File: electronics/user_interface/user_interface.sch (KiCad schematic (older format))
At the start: 87 parts, among them J1 Conn_01x06, J2 Conn_02x05_Odd_Even, SW1 ALPS_EC11E18244A5, U1 PCF8574, U2 PCF8574

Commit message: updated footprints to include 3dmodel of SOD-523 diode
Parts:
- N1: footprint Symbols:OSHW-Symbol_6.7x6mm_SilkScreen -> Symbol:OSHW-Symbol_6.7x6mm_SilkScreen
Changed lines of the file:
@@
 F 0 "N1" H 9450 6150 60  0000 C CNN
 F 1 "OHWLOGO" H 9450 5850 60  0000 C CNN
-F 2 "Symbols:OSHW-Symbol_6.7x6mm_SilkScreen" H 9450 6000 60  0001 C CNN
+F 2 "Symbol:OSHW-Symbol_6.7x6mm_SilkScreen" H 9450 6000 60  0001 C CNN
 F 3 "" H 9450 6000 60  0001 C CNN
 	1    9450 6000

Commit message: updated versionnumber
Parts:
- N2: value V20200517 -> V20200521
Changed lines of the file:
@@
 P 9450 6350
 F 0 "N2" H 9450 6450 60  0000 C CNN
-F 1 "V20200517" H 9450 6350 60  0000 C CNN
+F 1 "V20200521" H 9450 6350 60  0000 C CNN
 F 2 "SquantorLabels:Label_Generic" H 9450 6350 60  0001 C CNN
 F 3 "" H 9450 6350 60  0001 C CNN

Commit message: added pullup resistors, updated versionnumber
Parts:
- added R? (x2): 4.7K, SquantorRcl:R_0603_hand, symbol Device:R
- N2: value V20200521 -> V20200522
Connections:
- net SCL: now also R?.1
- net SDA: now also R?.1
- net VDD: now also R?.2, R?.2
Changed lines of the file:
@@
 P 9450 6350
 F 0 "N2" H 9450 6450 60  0000 C CNN
-F 1 "V20200521" H 9450 6350 60  0000 C CNN
+F 1 "V20200522" H 9450 6350 60  0000 C CNN
 F 2 "SquantorLabels:Label_Generic" H 9450 6350 60  0001 C CNN
 F 3 "" H 9450 6350 60  0001 C CNN
@@
 Wire Notes Line
 	2100 2400 2100 2550
+Text Label 2700 2150 0    50   ~ 0
+SDA
+Text Label 2700 2250 0    50   ~ 0
+SCL
+$Comp
+L Device:R R?
+U 1 1 5EC93454
+P 2500 2150
+F 0 "R?" V 2450 2000 50  0000 C CNN
+F 1 "4.7K" V 2500 2150 50  0000 C CNN
+F 2 "SquantorRcl:R_0603_hand" V 2430 2150 50  0001 C CNN
+F 3 "~" H 2500 2150 50  0001 C CNN
+	1    2500 2150
+	0    1    1    0
+$EndComp
+$Comp
+L Device:R R?
+U 1 1 5EC9375B
+P 2500 2250
+F 0 "R?" V 2450 2100 50  0000 C CNN
+F 1 "4.7K" V 2500 2250 50  0000 C CNN
+F 2 "SquantorRcl:R_0603_hand" V 2430 2250 50  0001 C CNN
+F 3 "~" H 2500 2250 50  0001 C CNN
+	1    2500 2250
+	0    1    1    0
+$EndComp
+Text Label 2300 2150 2    50   ~ 0
+VDD
+Text Label 2300 2250 2    50   ~ 0
+VDD
+Wire Wire Line
+	2300 2150 2350 2150
+Wire Wire Line
+	2350 2250 2300 2250
+Wire Wire Line
+	2700 2150 2650 2150
+Wire Wire Line
+	2650 2250 2700 2250
 $EndSCHEMATC

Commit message: routing completed
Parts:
- added R46: 4.7K, SquantorRcl:R_0603_hand, symbol Device:R
- gave numbers to parts that had none: 2
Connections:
- net !INT: now also R46.1
- net VDD: now also R46.2
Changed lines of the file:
@@
 SCL
 $Comp
-L Device:R R?
+L Device:R R44
 U 1 1 5EC93454
 P 2500 2150
-F 0 "R?" V 2450 2000 50  0000 C CNN
+F 0 "R44" V 2450 2000 50  0000 C CNN
 F 1 "4.7K" V 2500 2150 50  0000 C CNN
 F 2 "SquantorRcl:R_0603_hand" V 2430 2150 50  0001 C CNN
@@
 $EndComp
 $Comp
-L Device:R R?
+L Device:R R45
 U 1 1 5EC9375B
 P 2500 2250
-F 0 "R?" V 2450 2100 50  0000 C CNN
+F 0 "R45" V 2450 2100 50  0000 C CNN
 F 1 "4.7K" V 2500 2250 50  0000 C CNN
 F 2 "SquantorRcl:R_0603_hand" V 2430 2250 50  0001 C CNN
@@
 Wire Wire Line
 	2650 2250 2700 2250
+$Comp
+L Device:R R46
+U 1 1 5ED00DE2
+P 2500 2350
+F 0 "R46" V 2450 2200 50  0000 C CNN
+F 1 "4.7K" V 2500 2350 50  0000 C CNN
+F 2 "SquantorRcl:R_0603_hand" V 2430 2350 50  0001 C CNN
+F 3 "~" H 2500 2350 50  0001 C CNN
+	1    2500 2350
+	0    1    1    0
+$EndComp
+Text Label 2700 2350 0    50   ~ 0
+!INT
+Text Label 2300 2350 2    50   ~ 0
+VDD
+Wire Wire Line
+	2300 2350 2350 2350
+Wire Wire Line
+	2650 2350 2700 2350
 $EndSCHEMATC

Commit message: updated versionnumber, changed address selection tracks so you could disconnect them by cutting traces
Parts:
- N2: value V20200522 -> V20200524
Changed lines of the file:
@@
 P 9450 6350
 F 0 "N2" H 9450 6450 60  0000 C CNN
-F 1 "V20200522" H 9450 6350 60  0000 C CNN
+F 1 "V20200524" H 9450 6350 60  0000 C CNN
 F 2 "SquantorLabels:Label_Generic" H 9450 6350 60  0001 C CNN
 F 3 "" H 9450 6350 60  0001 C CNN

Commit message: added buzzer circuit
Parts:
- added BZ1: Buzzer, Buzzer_Beeper:Buzzer_12x9.5RM7.6, symbol Device:Buzzer
- N2: value V20200524 -> V20200602
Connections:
- net VDD: now also BZ1.1 (-); no longer R25.1
- new net Buzzer: BZ1.2 (+), R25.1
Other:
- moved on the sheet: R25
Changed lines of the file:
@@
 P 9450 6350
 F 0 "N2" H 9450 6450 60  0000 C CNN
-F 1 "V20200524" H 9450 6350 60  0000 C CNN
+F 1 "V20200602" H 9450 6350 60  0000 C CNN
 F 2 "SquantorLabels:Label_Generic" H 9450 6350 60  0001 C CNN
 F 3 "" H 9450 6350 60  0001 C CNN
@@
 	1    0    0    -1
 $EndComp
-Text Label 10800 3800 0    50   ~ 0
-VDD
 Wire Wire Line
 	10150 3900 10100 3900
@@
 	11000 3150 11000 5600
 Wire Wire Line
-	10100 3800 10450 3800
-Wire Wire Line
-	10750 3800 10800 3800
+	10100 3800 10200 3800
+Wire Wire Line
+	10500 3800 10550 3800
 $Comp
 L Device:R R25
 U 1 1 5ED82CF1
-P 10600 3800
-F 0 "R25" V 10550 3650 50  0000 C CNN
-F 1 "4.7K" V 10600 3800 50  0000 C CNN
-F 2 "SquantorRcl:R_0603_hand" V 10530 3800 50  0001 C CNN
-F 3 "~" H 10600 3800 50  0001 C CNN
-	1    10600 3800
+P 10350 3800
+F 0 "R25" V 10300 3650 50  0000 C CNN
+F 1 "4.7K" V 10350 3800 50  0000 C CNN
+F 2 "SquantorRcl:R_0603_hand" V 10280 3800 50  0001 C CNN
+F 3 "~" H 10350 3800 50  0001 C CNN
+	1    10350 3800
 	0    1    1    0
 $EndComp
@@
 Wire Wire Line
 	2650 2350 2700 2350
+$Comp
+L Device:Buzzer BZ1
+U 1 1 5ED89C6E
+P 6250 6950
+F 0 "BZ1" H 6402 6979 50  0000 L CNN
+F 1 "Buzzer" H 6402 6888 50  0000 L CNN
+F 2 "Buzzer_Beeper:Buzzer_12x9.5RM7.6" V 6225 7050 50  0001 C CNN
+F 3 "~" V 6225 7050 50  0001 C CNN
+	1    6250 6950
+	1    0    0    -1
+$EndComp
+Text Label 6100 6850 2    50   ~ 0
+VDD
+Wire Wire Line
+	6100 6850 6150 6850
+Text Label 10550 3800 0    50   ~ 0
+Buzzer
+Text Label 6100 7050 2    50   ~ 0
+Buzzer
+Wire Wire Line
+	6100 7050 6150 7050
 $EndSCHEMATC

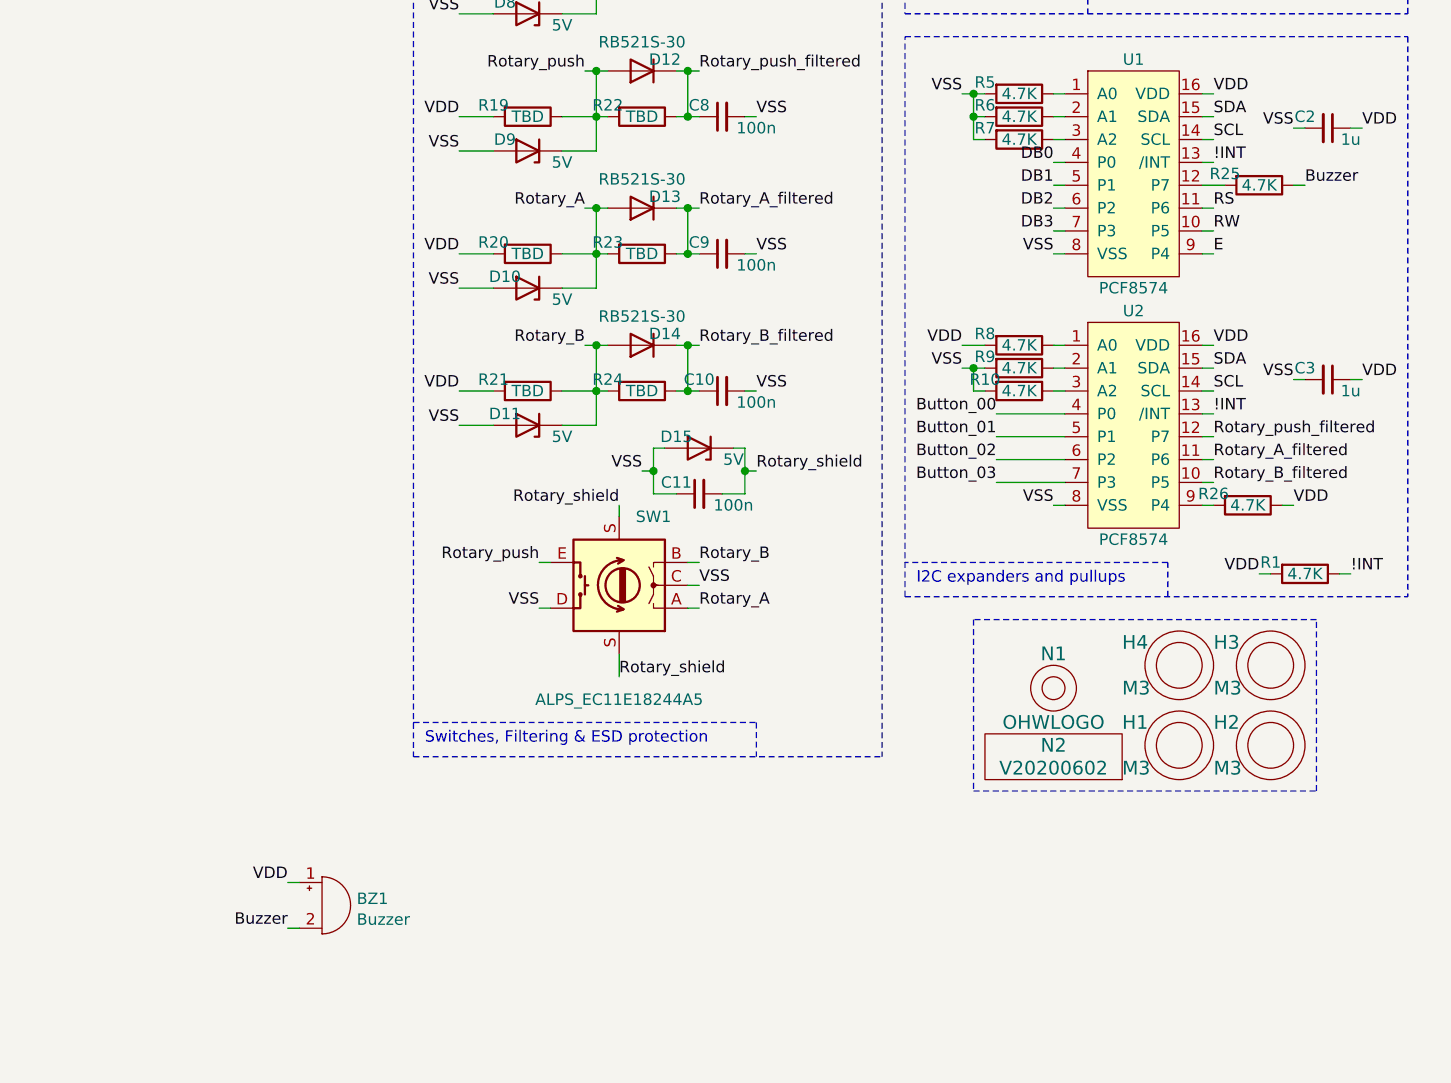
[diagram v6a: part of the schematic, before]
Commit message: prettyfied the buzzer circuit
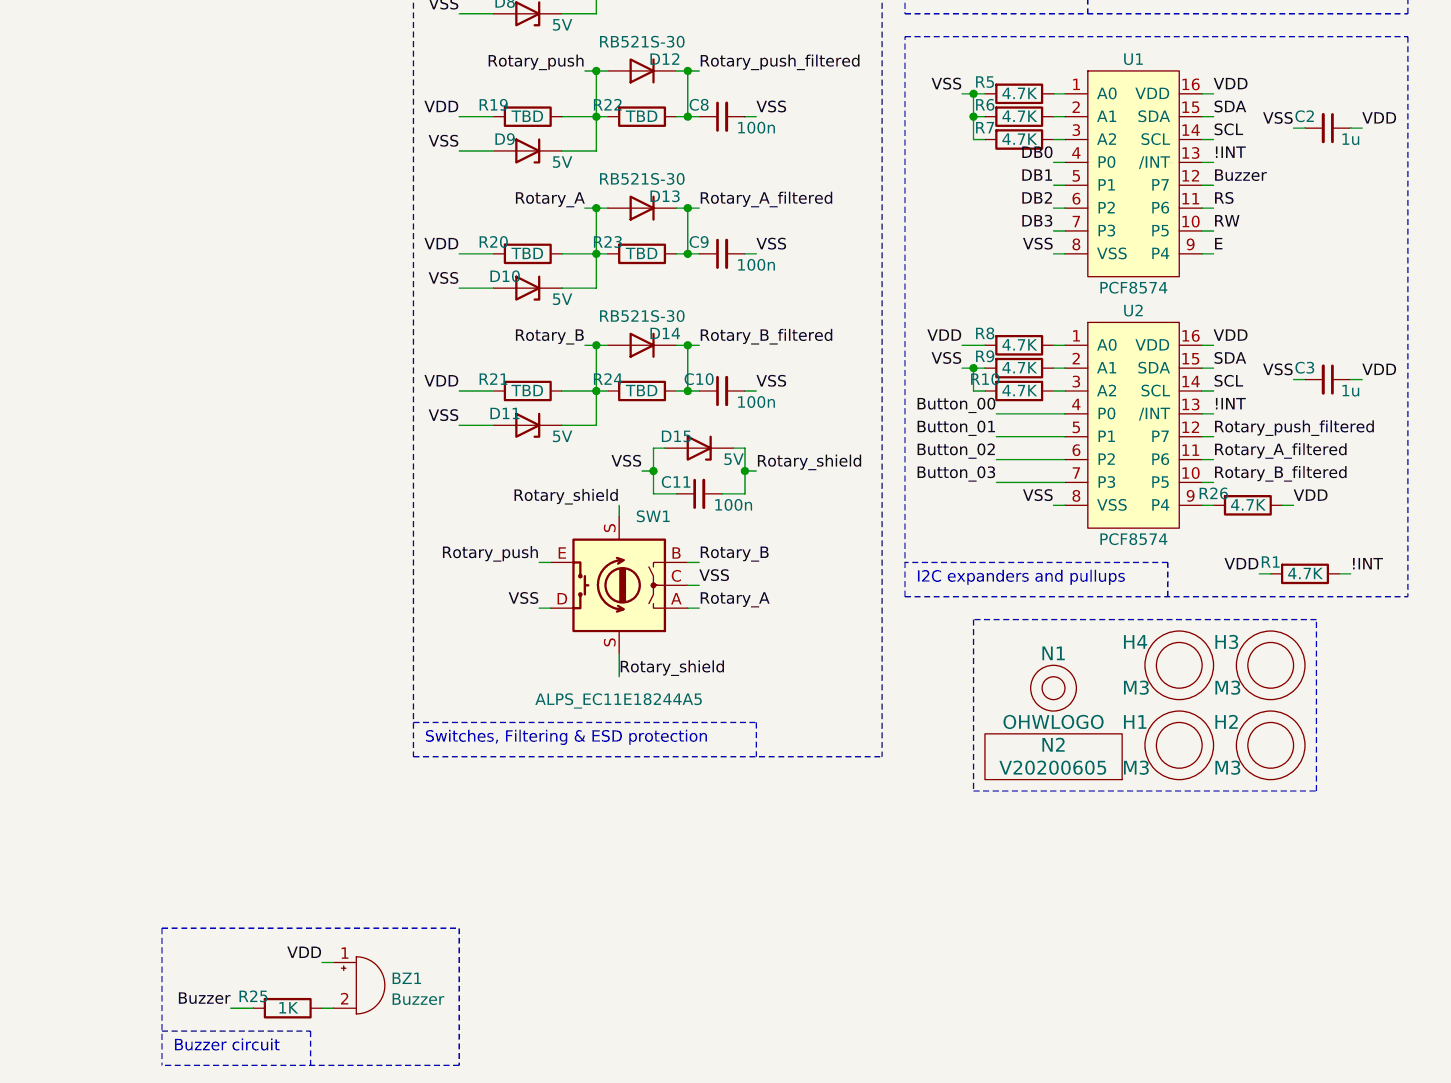
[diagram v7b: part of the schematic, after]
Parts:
- N2: value V20200602 -> V20200605
- R25: value 4.7K -> 1K
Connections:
- net Buzzer: now also R25.2, U1.12 (P7); no longer BZ1.2 (+), R25.1
- new net: BZ1.2 (+), R25.1
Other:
- note added: "Buzzer circuit"
- moved on the sheet: BZ1, R25
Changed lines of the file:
@@
 P 9450 6350
 F 0 "N2" H 9450 6450 60  0000 C CNN
-F 1 "V20200602" H 9450 6350 60  0000 C CNN
+F 1 "V20200605" H 9450 6350 60  0000 C CNN
 F 2 "SquantorLabels:Label_Generic" H 9450 6350 60  0001 C CNN
 F 3 "" H 9450 6350 60  0001 C CNN
@@
 Wire Notes Line
 	11000 3150 11000 5600
-Wire Wire Line
-	10100 3800 10200 3800
-Wire Wire Line
-	10500 3800 10550 3800
 $Comp
 L Device:R R25
 U 1 1 5ED82CF1
-P 10350 3800
-F 0 "R25" V 10300 3650 50  0000 C CNN
-F 1 "4.7K" V 10350 3800 50  0000 C CNN
-F 2 "SquantorRcl:R_0603_hand" V 10280 3800 50  0001 C CNN
-F 3 "~" H 10350 3800 50  0001 C CNN
-	1    10350 3800
+P 6100 7400
+F 0 "R25" V 6050 7250 50  0000 C CNN
+F 1 "1K" V 6100 7400 50  0000 C CNN
+F 2 "SquantorRcl:R_0603_hand" V 6030 7400 50  0001 C CNN
+F 3 "~" H 6100 7400 50  0001 C CNN
+	1    6100 7400
 	0    1    1    0
 $EndComp
@@
 L Device:Buzzer BZ1
 U 1 1 5ED89C6E
-P 6250 6950
-F 0 "BZ1" H 6402 6979 50  0000 L CNN
-F 1 "Buzzer" H 6402 6888 50  0000 L CNN
-F 2 "Buzzer_Beeper:Buzzer_12x9.5RM7.6" V 6225 7050 50  0001 C CNN
-F 3 "~" V 6225 7050 50  0001 C CNN
-	1    6250 6950
+P 6400 7300
+F 0 "BZ1" H 6552 7329 50  0000 L CNN
+F 1 "Buzzer" H 6552 7238 50  0000 L CNN
+F 2 "Buzzer_Beeper:Buzzer_12x9.5RM7.6" V 6375 7400 50  0001 C CNN
+F 3 "~" V 6375 7400 50  0001 C CNN
+	1    6400 7300
 	1    0    0    -1
 $EndComp
-Text Label 6100 6850 2    50   ~ 0
-VDD
-Wire Wire Line
-	6100 6850 6150 6850
-Text Label 10550 3800 0    50   ~ 0
+Text Label 6250 7200 2    50   ~ 0
+VDD
+Wire Wire Line
+	6250 7200 6300 7200
+Text Label 10150 3800 0    50   ~ 0
 Buzzer
-Text Label 6100 7050 2    50   ~ 0
+Wire Wire Line
+	10100 3800 10150 3800
+Text Label 5850 7400 2    50   ~ 0
 Buzzer
 Wire Wire Line
-	6100 7050 6150 7050
+	5850 7400 5950 7400
+Wire Wire Line
+	6250 7400 6300 7400
+Text Notes 5600 7600 0    50   ~ 0
+Buzzer circuit
+Wire Notes Line
+	5550 7050 6850 7050
+Wire Notes Line
+	6850 7650 5550 7650
+Wire Notes Line
+	5550 7050 5550 7650
+Wire Notes Line
+	6850 7050 6850 7650
+Wire Notes Line
+	6200 7500 6200 7650
+Wire Notes Line
+	5550 7500 6200 7500
 $EndSCHEMATC
